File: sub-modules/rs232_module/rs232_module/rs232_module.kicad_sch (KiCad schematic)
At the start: 12 parts, among them J1 Conn_02x06_Odd_Even, J9 MPT 0,5/ 6-2,54, U1 ADM3312EARUZ-REEL7

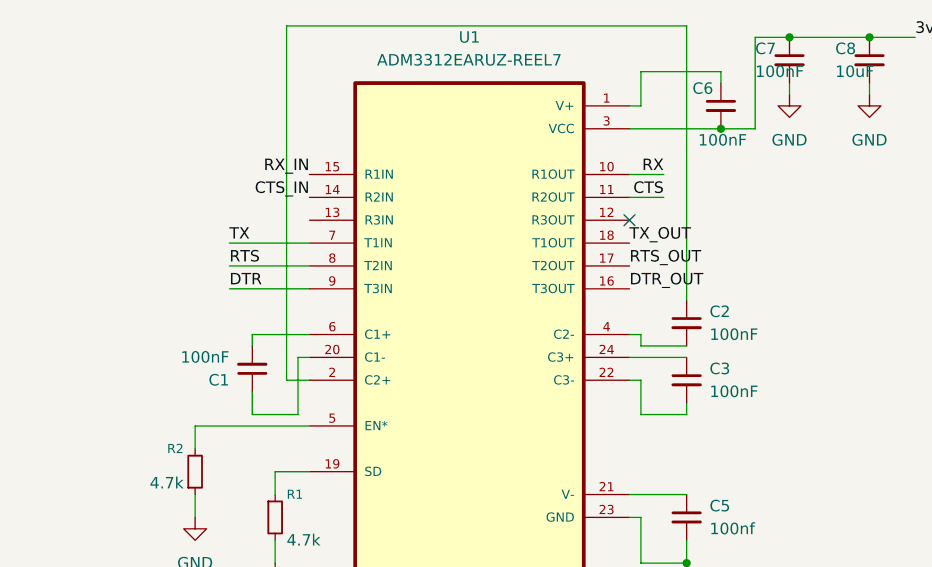
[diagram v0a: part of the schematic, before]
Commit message: Update schematics after moving to KiCad 10
Added some footprints to a local lib, as the silkscreen caused issues.

Signed-off-by: Marc Kelly <mpkelly@achenar.co.uk>
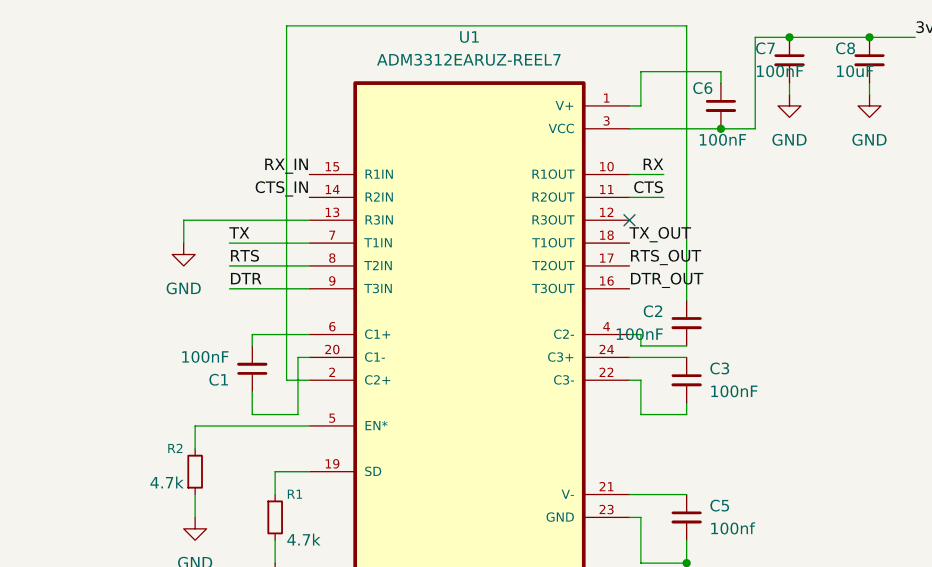
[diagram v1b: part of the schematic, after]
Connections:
- net GND: now also U1.13 (R3IN)

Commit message: Sorting out BOMs
Signed-off-by: Marc Kelly <mpkelly@achenar.co.uk>
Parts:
- C1, C2, C3, C6, C7: MFN (none) -> Generic X7R; MFP (none) -> 100nF; SUPPLIER (none) -> Mouser; SUPPLIER_PN (none) -> 581-06035C104JAT2A62
- C5: value 100nf -> 100nF; MFN (none) -> Generic X7R; MFP (none) -> 100nF; SUPPLIER (none) -> Mouser; SUPPLIER_PN (none) -> 581-06035C104JAT2A62
- C8: SUPPLIER (none) -> Mouser; SUPPLIER_PN (none) -> 80-T491T106K010
- J1: MFN (none) -> Wurth; MFP (none) -> 613012243121; SUPPLIER (none) -> Mouser; SUPPLIER_PN (none) -> 710-613012243121
- J9: SUPPLIER (none) -> Mouser; SUPPLIER_PN (none) -> 651-1725698
- R1, R2: MFN (none) -> Generic; MFP (none) -> 4.7k 1%; SUPPLIER (none) -> Mouser; SUPPLIER_PN (none) -> 594-MCT06030C4701FP5
- U1: MFN (none) -> Analog Devices; MFP (none) -> ADM3312EARUZR7; SUPPLIER (none) -> Mouser; SUPPLIER_PN (none) -> 584-ADM3312EARUZR7
